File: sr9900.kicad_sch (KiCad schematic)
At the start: 1 part

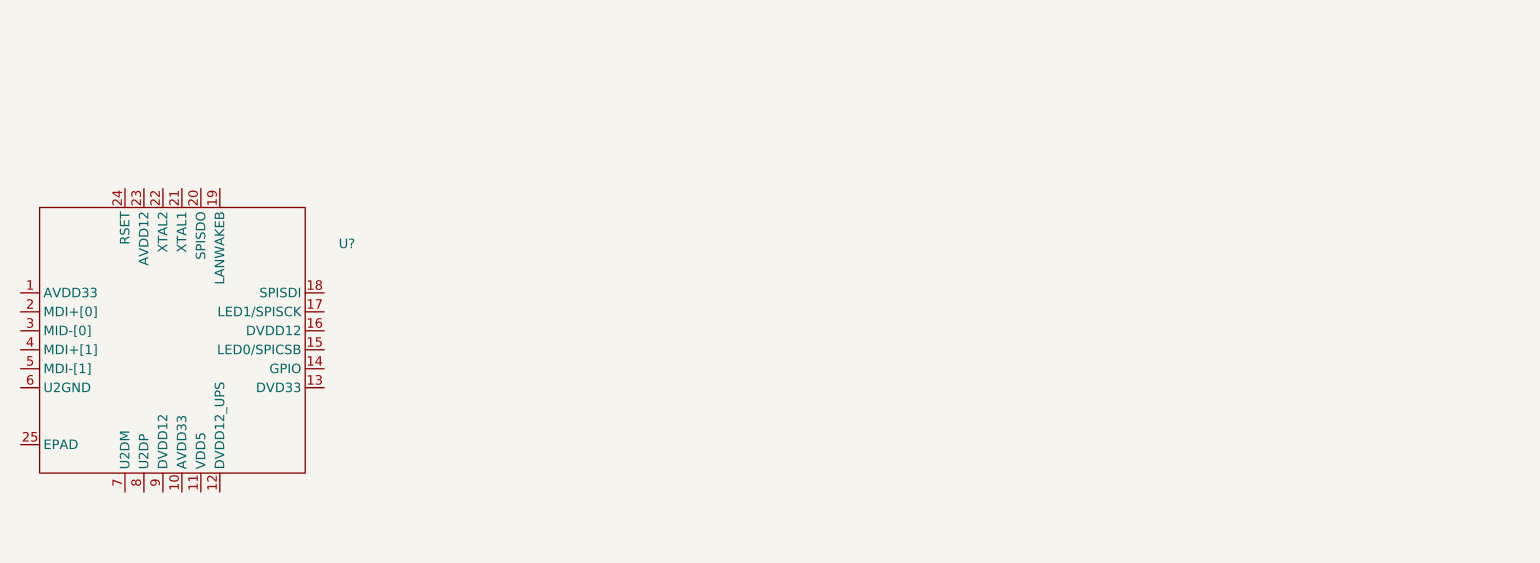
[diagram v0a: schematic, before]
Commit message: add RJ45 Symbol
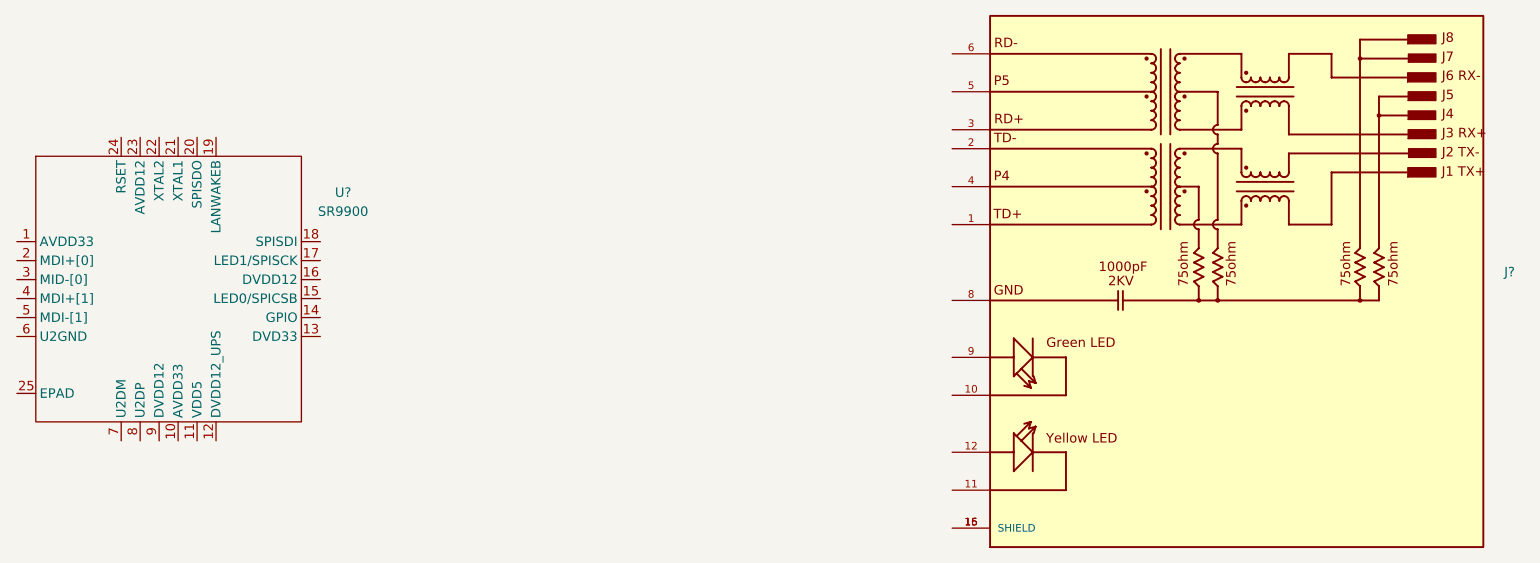
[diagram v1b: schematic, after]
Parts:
- added J?: (no value), symbol sr9900:HR911105A
- U?: value (none) -> SR9900; footprint (none) -> Package_DFN_QFN:QFN-24-1EP_4x4mm_P0.5mm_EP2.7x2.7mm
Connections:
- new net: J?.15 (SHIELD), J?.16 (SHIELD)
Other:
- moved on the sheet: U?
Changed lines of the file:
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@@
     (rev "V1.0")
   )
-  (symbol (lib_id "sr9900:SR9900") (at 45.212 66.802 0) (unit 1)
+  (symbol (lib_id "sr9900:SR9900") (at 44.704 59.944 0) (unit 1)
     (in_bom yes) (on_board yes) (fields_autoplaced)
-    (property "Reference" "U?" (id 0) (at 86.36 71.6532 0))
-    (property "Value" "" (id 1) (at 86.36 74.1932 0))
-    (property "Footprint" "" (id 2) (at 45.212 66.802 0)
+    (property "Reference" "U?" (id 0) (at 85.852 64.7952 0))
+    (property "Value" "SR9900" (id 1) (at 85.852 67.3352 0))
+    (property "Footprint" "Package_DFN_QFN:QFN-24-1EP_4x4mm_P0.5mm_EP2.7x2.7mm" (id 2) (at 44.704 59.944 0)
       (effects (font (size 1.27 1.27)) hide)
     )
-    (property "Datasheet" "http://www.corechip-sz.com/download.asp" (id 3) (at 45.212 66.802 0)
+    (property "Datasheet" "http://www.corechip-sz.com/download.asp" (id 3) (at 44.704 59.944 0)
       (effects (font (size 1.27 1.27)) hide)
     )
@@
     (pin "9")
   )
+  (symbol (lib_id "sr9900:HR911105A") (at 205.486 76.708 0) (unit 1)
+    (in_bom yes) (on_board yes) (fields_autoplaced)
+    (property "Reference" "J?" (id 0) (at 241.3 75.4379 0)
+      (effects (font (size 1.27 1.27)) (justify left))
+    )
+    (property "Value" "" (id 1) (at 241.3 77.9779 0)
+      (effects (font (size 1.27 1.27)) (justify left))
+    )
+    (property "Footprint" "" (id 2) (at 205.486 76.708 0)
+      (effects (font (size 1.27 1.27)) (justify left bottom) hide)
+    )
+    (property "Datasheet" "" (id 3) (at 205.486 76.708 0)
+      (effects (font (size 1.27 1.27)) (justify left bottom) hide)
+    )
+    (property "PACKAGE" "None" (id 4) (at 205.486 76.708 0)
+      (effects (font (size 1.27 1.27)) (justify left bottom) hide)
+    )
+    (property "STANDARD" "Manufacturer Recommendation" (id 5) (at 205.486 76.708 0)
+      (effects (font (size 1.27 1.27)) (justify left bottom) hide)
+    )
+    (property "PRICE" "None" (id 6) (at 205.486 76.708 0)
+      (effects (font (size 1.27 1.27)) (justify left bottom) hide)
+    )
+    (property "PARTREV" "A" (id 7) (at 205.486 76.708 0)
+      (effects (font (size 1.27 1.27)) (justify left bottom) hide)
+    )
+    (property "MF" "HanRun" (id 8) (at 205.486 76.708 0)
+      (effects (font (size 1.27 1.27)) (justify left bottom) hide)
+    )
+    (property "MP" "HR911105A" (id 9) (at 205.486 76.708 0)
+      (effects (font (size 1.27 1.27)) (justify left bottom) hide)
+    )
+    (property "AVAILABILITY" "Unavailable" (id 10) (at 205.486 76.708 0)
+      (effects (font (size 1.27 1.27)) (justify left bottom) hide)
+    )
+    (property "DESCRIPTION" "DIP RJ45 Connector;" (id 11) (at 205.486 76.708 0)
+      (effects (font (size 1.27 1.27)) (justify left bottom) hide)
+    )
+    (pin "1")
+    (pin "10")
+    (pin "11")
+    (pin "12")
+    (pin "15")
+    (pin "16")
+    (pin "2")
+    (pin "3")
+    (pin "4")
+    (pin "5")
+    (pin "6")
+    (pin "8")
+    (pin "9")
+  )
   (sheet_instances
     (path "/" (page "1"))
   )
   (symbol_instances
+    (path "/fbe5f378-9338-46c4-9310-0e94bfbd7e98"
+      (reference "J?") (unit 1) (value "HR911105A") (footprint "Library:Hanrun_HR911105A")
+    )
     (path "/4c667c01-9714-47fe-9fa0-01f70b232f05"
       (reference "U?") (unit 1) (value "SR9900") (footprint "Package_DFN_QFN:QFN-24-1EP_4x4mm_P0.5mm_EP2.7x2.7mm")

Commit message: update
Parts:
- added C? (x10): C_Small, symbol Device:C_Small
- added FB? (x2): FerriteBead_Small, symbol Device:FerriteBead_Small
- added J?: USB_B_Micro, Connector_USB:USB_Micro-B_Molex_47346-0001, symbol Connector:USB_B_Micro
- added R? (x5): R_Small, symbol Device:R_Small
- added Y? (x2): Crystal_Small, symbol Device:Crystal_Small
- J?: value (none) -> HR911105A; footprint (none) -> Library:Hanrun_HR911105A
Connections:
- net VDD33: now reaches U?.1 (AVDD33)
- net VDD33: now also C?.2
- net at U?.13 (DVD33): now also C?.2
- net at U?.14 (GPIO): now also R?.2
- net LINK_LED: now reaches U?.15 (LED0/SPICSB)
- net at U?.16 (DVDD12): now also C?.1
- net SPEED_LED: now reaches U?.17 (LED1/SPISCK)
- net at U?.19 (LANWAKEB): now also R?.1
- net TX_P: now reaches U?.2 (MDI+[0])
- net XIN: now reaches U?.21 (XTAL1)
- net XIN: now also C?.2, Y?.2
- net XOUT: now reaches U?.22 (XTAL2)
- net XOUT: now also C?.2, Y?.1
- net VDD12: now reaches U?.23 (AVDD12)
- net VDD12: now also C?.2
- net at U?.24 (RSET): now also R?.2
- net GND: now reaches U?.25 (EPAD)
- net GND: now also U?.6 (U2GND), C?.1, C?.1, C?.1, C?.1, C?.1, C?.1, C?.2, C?.2, C?.2, J?.5 (GND), R?.1, R?.1
- net TX_N: now reaches U?.3 (MID-[0])
- net RX_P: now reaches U?.4 (MDI+[1])
- net RX_N: now reaches U?.5 (MDI-[1])
- net USB_D-: now reaches U?.7 (U2DM)
- net USB_D-: now also J?.2 (D-)
- net USB_D+: now reaches U?.8 (U2DP)
- net USB_D+: now also J?.3 (D+)
- new net: FB?.1, J?.1 (VBUS)
- new net +5V: C?.1, C?.1, FB?.2
- new net GND1: C?.2, J?.6 (Shield), R?.2
- no-connect marks 0 -> 3
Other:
- moved on the sheet: U?

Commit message: add more
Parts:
- removed C?: C_Small, symbol Device:C_Small
- removed FB?: FerriteBead_Small, symbol Device:FerriteBead_Small
- removed R?: R_Small, symbol Device:R_Small
- removed Y?: Crystal_Small, symbol Device:Crystal_Small
- added C? (x7): C_Small, symbol Device:C_Small
- added R? (x2): R_Small, symbol Device:R_Small
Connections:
- net RX_N is gone; now on net RD-: U?.5 (MDI-[1])
- net RX_P is gone; now on net RD+: U?.4 (MDI+[1])
- net TX_N is gone; now on net TD-: U?.3 (MID-[0])
- net TX_P is gone; now on net TD+: U?.2 (MDI+[0])
- net +5V: now also U?.11 (VDD5)
- net GND: now also C?.1, C?.1, C?.1, C?.1, C?.1, C?.2, C?.2
- net GND1: now also J?.15 (SHIELD), J?.16 (SHIELD), J?.8
- net LINK_LED: now also J?.11
- net SPEED_LED: now also J?.10
- net VDD12: now also C?.1, U?.16 (DVDD12), U?.9 (DVDD12), C?.1, C?.1
- net VDD33: now also C?.2, U?.10 (AVDD33), U?.13 (DVD33), C?.2, C?.2
- net at U?.12 (DVDD12_UPS): now also C?.2, C?.2
- net TD+: now reaches J?.1
- net at J?.12: now also R?.2
- net TD-: now reaches J?.2
- net RD+: now reaches J?.3
- net at J?.4: now also J?.5, C?.2
- net RD-: now reaches J?.6
- net at J?.9: now also R?.2
- new net: R?.1, R?.1
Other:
- moved on the sheet: C?, J?

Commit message: update doc
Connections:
- net +5V: no longer U?.11 (VDD5)
- no-connect marks 3 -> 4
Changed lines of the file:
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@@
   (no_connect (at 49.53 44.45))
   (no_connect (at 92.71 137.16))
+  (no_connect (at 76.2 163.83))
   (bus_entry (at 240.03 23.622) (size 2.54 2.54)
     (stroke (width 0) (type default) (color 0 0 0 0))
@@
     (stroke (width 0) (type default) (color 0 0 0 0))
   )
-  (wire (pts (xy 76.2 163.83) (xy 76.2 172.72))
-    (stroke (width 0) (type default) (color 0 0 0 0))
-  )
   (wire (pts (xy 64.77 44.45) (xy 64.77 50.8))
     (stroke (width 0) (type default) (color 0 0 0 0))
@@
   )
   (label "RD+" (at 172.72 54.61 0)
-    (effects (font (size 1.27 1.27)) (justify left bottom))
-  )
-  (label "+5V" (at 76.2 172.085 90)
     (effects (font (size 1.27 1.27)) (justify left bottom))
   )
@@
   (symbol (lib_id "sr9900:SR9900") (at 54.61 125.73 0) (unit 1)
     (in_bom yes) (on_board yes)
-    (property "Reference" "U?" (id 0) (at 50.8 127 0))
-    (property "Value" "SR9900" (id 1) (at 50.8 129.54 0))
+    (property "Reference" "U?" (id 0) (at 56.515 124.46 0))
+    (property "Value" "SR9900" (id 1) (at 57.785 163.195 0))
     (property "Footprint" "Package_DFN_QFN:QFN-24-1EP_4x4mm_P0.5mm_EP2.7x2.7mm" (id 2) (at 54.61 125.73 0)
       (effects (font (size 1.27 1.27)) hide)
